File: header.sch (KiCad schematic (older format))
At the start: 1 part, among them U1 ICE40HX4K-TQ144

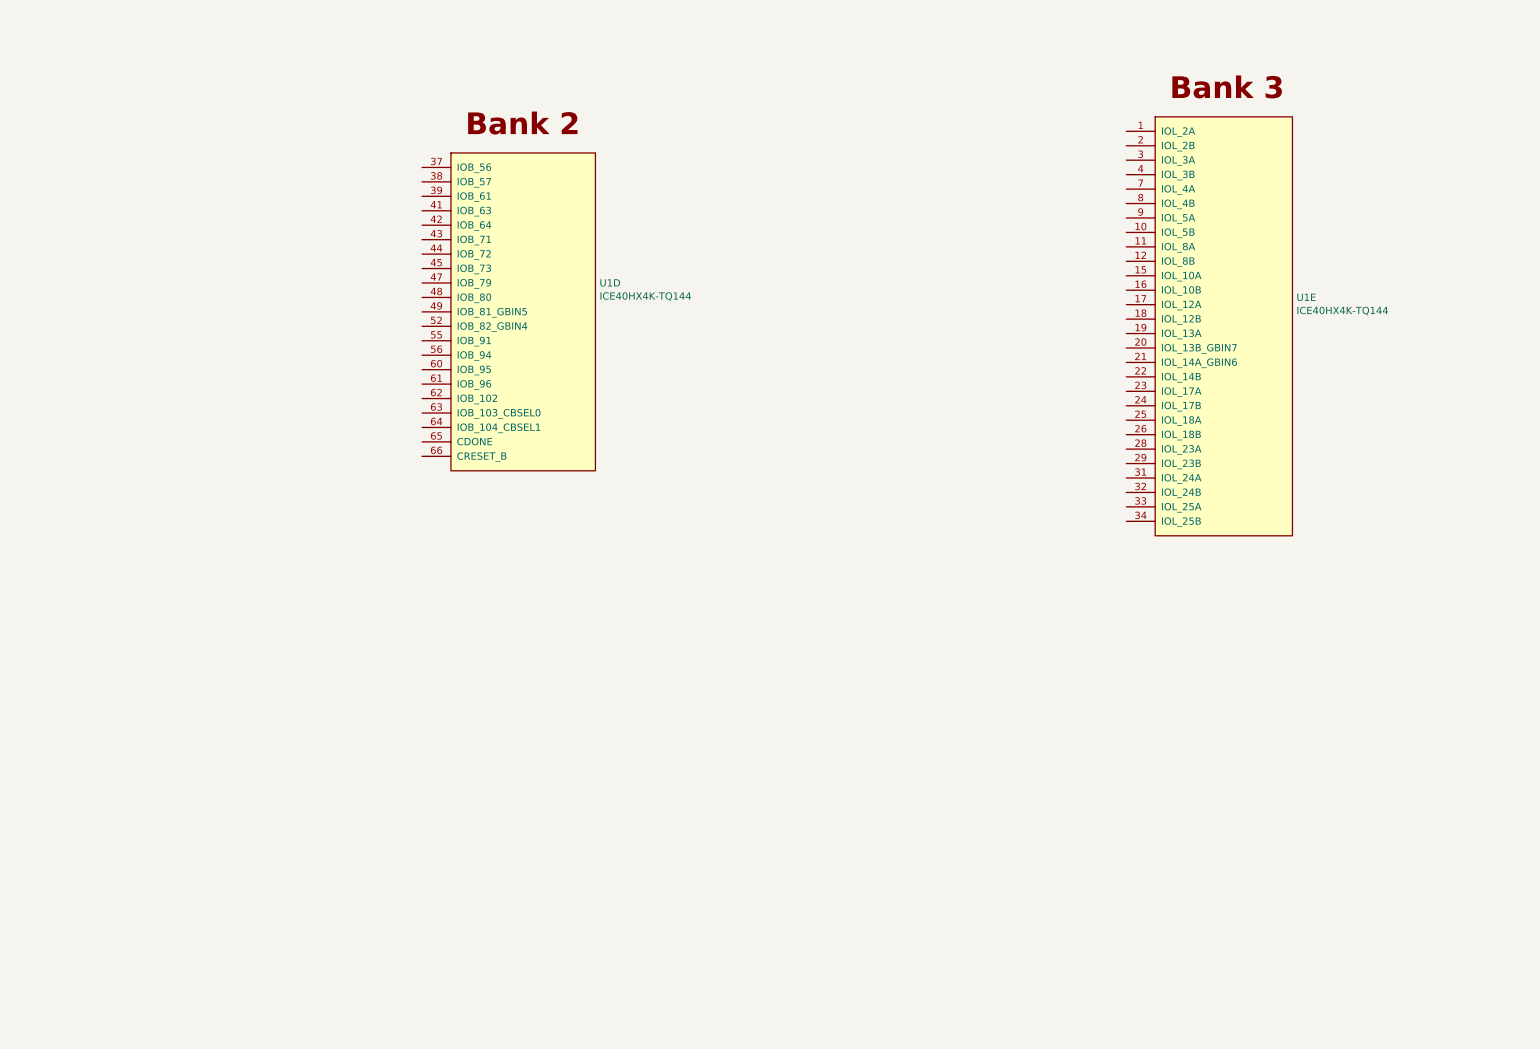
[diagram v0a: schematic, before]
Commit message: sram, ui, power, flash and header
SRAM: mostly done. Changed the choosen IC to a faster one in a differenc housing.

POWER: added some step down converter for 3.3 V and 1.2 V. The 1.2 V is oversized and could be changed to a smaller one

Programmer: added flash.

HEADER: Added Arduino Uno like headers with 5 V signal level. Analog is not connected now, will get an I2C ADC in future. Also added 3 digilent pmod styled connector with 3.3 V signal level.

UI: added 5 buttons and 8 LEDs. There is some space left over, maybe double the LED count in future.
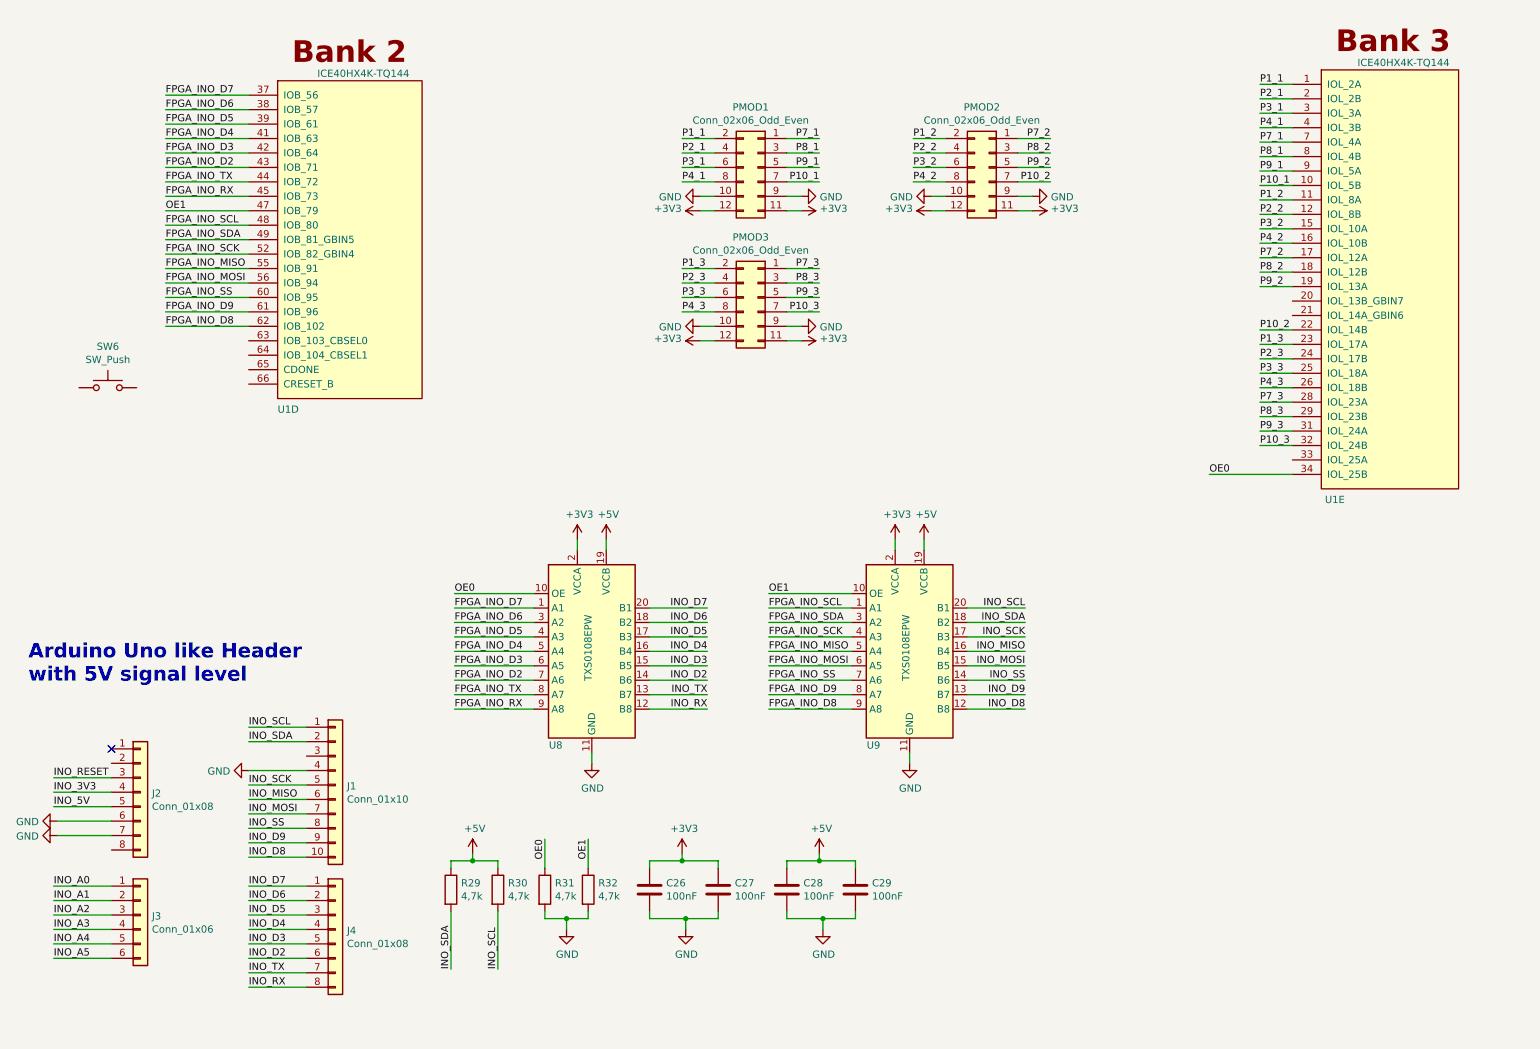
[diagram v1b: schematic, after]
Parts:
- added C26, C27, C28, C29: 100nF, Capacitor_SMD:C_0603_1608Metric, symbol Device:C
- added J1: Conn_01x10, Connector_PinSocket_2.54mm:PinSocket_1x10_P2.54mm_Vertical, symbol Connector_Generic:Conn_01x10
- added J2, J4: Conn_01x08, Connector_PinSocket_2.54mm:PinSocket_1x08_P2.54mm_Vertical, symbol Connector_Generic:Conn_01x08
- added J3: Conn_01x06, Connector_PinSocket_2.54mm:PinSocket_1x06_P2.54mm_Vertical, symbol Connector_Generic:Conn_01x06
- added PMOD1, PMOD2, PMOD3: Conn_02x06_Odd_Even, Connector_PinSocket_2.54mm:PinSocket_2x06_P2.54mm_Horizontal, symbol Connector_Generic:Conn_02x06_Odd_Even
- added R29, R30, R31, R32: 4,7k, Resistor_SMD:R_0603_1608Metric, symbol Device:R
- added SW6: SW_Push, footprints:SW_SPST_TL3305A, symbol Switch:SW_Push
- added U8, U9: TXS0108EPW, Package_SO:TSSOP-20_4.4x6.5mm_P0.65mm, symbol Logic_LevelTranslator:TXS0108EPW
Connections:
- net P1_1: now reaches U1.1 (IOL_2A)
- net P1_1: now also PMOD1.2 (Pin_2)
- net P10_1: now reaches U1.10 (IOL_5B)
- net P10_1: now also PMOD1.7 (Pin_7)
- net P1_2: now reaches U1.11 (IOL_8A)
- net P1_2: now also PMOD2.2 (Pin_2)
- net P2_2: now reaches U1.12 (IOL_8B)
- net P2_2: now also PMOD2.4 (Pin_4)
- net P3_2: now reaches U1.15 (IOL_10A)
- net P3_2: now also PMOD2.6 (Pin_6)
- net P4_2: now reaches U1.16 (IOL_10B)
- net P4_2: now also PMOD2.8 (Pin_8)
- net P7_2: now reaches U1.17 (IOL_12A)
- net P7_2: now also PMOD2.1 (Pin_1)
- net P8_2: now reaches U1.18 (IOL_12B)
- net P8_2: now also PMOD2.3 (Pin_3)
- net P9_2: now reaches U1.19 (IOL_13A)
- net P9_2: now also PMOD2.5 (Pin_5)
- net P2_1: now reaches U1.2 (IOL_2B)
- net P2_1: now also PMOD1.4 (Pin_4)
- net P10_2: now reaches U1.22 (IOL_14B)
- net P10_2: now also PMOD2.7 (Pin_7)
- net P1_3: now reaches U1.23 (IOL_17A)
- net P1_3: now also PMOD3.2 (Pin_2)
- net P2_3: now reaches U1.24 (IOL_17B)
- net P2_3: now also PMOD3.4 (Pin_4)
- net P3_3: now reaches U1.25 (IOL_18A)
- net P3_3: now also PMOD3.6 (Pin_6)
- net P4_3: now reaches U1.26 (IOL_18B)
- net P4_3: now also PMOD3.8 (Pin_8)
- net P7_3: now reaches U1.28 (IOL_23A)
- net P7_3: now also PMOD3.1 (Pin_1)
- net P8_3: now reaches U1.29 (IOL_23B)
- net P8_3: now also PMOD3.3 (Pin_3)
- net P3_1: now reaches U1.3 (IOL_3A)
- net P3_1: now also PMOD1.6 (Pin_6)
- net P9_3: now reaches U1.31 (IOL_24A)
- net P9_3: now also PMOD3.5 (Pin_5)
- net P10_3: now reaches U1.32 (IOL_24B)
- net P10_3: now also PMOD3.7 (Pin_7)
- net OE0: now reaches U1.34 (IOL_25B)
- net OE0: now also R31.1, U8.10 (OE)
- net P4_1: now reaches U1.4 (IOL_3B)
- net P4_1: now also PMOD1.8 (Pin_8)
- net P7_1: now reaches U1.7 (IOL_4A)
- net P7_1: now also PMOD1.1 (Pin_1)
- net P8_1: now reaches U1.8 (IOL_4B)
- net P8_1: now also PMOD1.3 (Pin_3)
- net P9_1: now reaches U1.9 (IOL_5A)
- net P9_1: now also PMOD1.5 (Pin_5)
- net FPGA_INO_D7: now reaches U1.37 (IOB_56)
- net FPGA_INO_D7: now also U8.1 (A1)
- net FPGA_INO_D6: now reaches U1.38 (IOB_57)
- net FPGA_INO_D6: now also U8.3 (A2)
- net FPGA_INO_D5: now reaches U1.39 (IOB_61)
- net FPGA_INO_D5: now also U8.4 (A3)
- net FPGA_INO_D4: now reaches U1.41 (IOB_63)
- net FPGA_INO_D4: now also U8.5 (A4)
- net FPGA_INO_D3: now reaches U1.42 (IOB_64)
- net FPGA_INO_D3: now also U8.6 (A5)
- net FPGA_INO_D2: now reaches U1.43 (IOB_71)
- net FPGA_INO_D2: now also U8.7 (A6)
- net FPGA_INO_TX: now reaches U1.44 (IOB_72)
- net FPGA_INO_TX: now also U8.8 (A7)
- net FPGA_INO_RX: now reaches U1.45 (IOB_73)
- net FPGA_INO_RX: now also U8.9 (A8)
- net OE1: now reaches U1.47 (IOB_79)
- net OE1: now also R32.1, U9.10 (OE)
- net FPGA_INO_SCL: now reaches U1.48 (IOB_80)
- net FPGA_INO_SCL: now also U9.1 (A1)
- net FPGA_INO_SDA: now reaches U1.49 (IOB_81_GBIN5)
- net FPGA_INO_SDA: now also U9.3 (A2)
- net FPGA_INO_SCK: now reaches U1.52 (IOB_82_GBIN4)
- net FPGA_INO_SCK: now also U9.4 (A3)
- net FPGA_INO_MISO: now reaches U1.55 (IOB_91)
- net FPGA_INO_MISO: now also U9.5 (A4)
- net FPGA_INO_MOSI: now reaches U1.56 (IOB_94)
- net FPGA_INO_MOSI: now also U9.6 (A5)
- net FPGA_INO_SS: now reaches U1.60 (IOB_95)
- net FPGA_INO_SS: now also U9.7 (A6)
- net FPGA_INO_D9: now reaches U1.61 (IOB_96)
- net FPGA_INO_D9: now also U9.8 (A7)
- net FPGA_INO_D8: now reaches U1.62 (IOB_102)
- net FPGA_INO_D8: now also U9.9 (A8)
- new net +3V3: C26.1, C27.1, PMOD1.11 (Pin_11), PMOD1.12 (Pin_12), PMOD2.11 (Pin_11), PMOD2.12 (Pin_12), PMOD3.11 (Pin_11), PMOD3.12 (Pin_12), U8.2 (VCCA), U9.2 (VCCA)
- new net +5V: C28.1, C29.1, R29.1, R30.1, U8.19 (VCCB), U9.19 (VCCB)
- new net GND: C26.2, C27.2, C28.2, C29.2, J1.4 (Pin_4), J2.6 (Pin_6), J2.7 (Pin_7), PMOD1.10 (Pin_10), PMOD1.9 (Pin_9), PMOD2.10 (Pin_10), PMOD2.9 (Pin_9), PMOD3.10 (Pin_10), PMOD3.9 (Pin_9), R31.2, R32.2, U8.11 (GND), U9.11 (GND)
- new net INO_3V3: J2.4 (Pin_4)
- new net INO_5V: J2.5 (Pin_5)
- new net INO_A0: J3.1 (Pin_1)
- new net INO_A1: J3.2 (Pin_2)
- new net INO_A2: J3.3 (Pin_3)
- new net INO_A3: J3.4 (Pin_4)
- new net INO_A4: J3.5 (Pin_5)
- new net INO_A5: J3.6 (Pin_6)
- new net INO_D2: J4.6 (Pin_6), U8.14 (B6)
- new net INO_D3: J4.5 (Pin_5), U8.15 (B5)
- new net INO_D4: J4.4 (Pin_4), U8.16 (B4)
- new net INO_D5: J4.3 (Pin_3), U8.17 (B3)
- new net INO_D6: J4.2 (Pin_2), U8.18 (B2)
- new net INO_D7: J4.1 (Pin_1), U8.20 (B1)
- new net INO_D8: J1.10 (Pin_10), U9.12 (B8)
- new net INO_D9: J1.9 (Pin_9), U9.13 (B7)
- new net INO_MISO: J1.6 (Pin_6), U9.16 (B4)
- new net INO_MOSI: J1.7 (Pin_7), U9.15 (B5)
- new net INO_RESET: J2.3 (Pin_3)
- new net INO_RX: J4.8 (Pin_8), U8.12 (B8)
- new net INO_SCK: J1.5 (Pin_5), U9.17 (B3)
- new net INO_SCL: J1.1 (Pin_1), R30.2, U9.20 (B1)
- new net INO_SDA: J1.2 (Pin_2), R29.2, U9.18 (B2)
- new net INO_SS: J1.8 (Pin_8), U9.14 (B6)
- new net INO_TX: J4.7 (Pin_7), U8.13 (B7)
- no-connect marks 0 -> 1
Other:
- note added: "Arduino Uno like Header\nwith 5V signal level"
- moved on the sheet: U1D, U1E
